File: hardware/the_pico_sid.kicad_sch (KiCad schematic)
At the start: 12 parts, among them J1 SWD, U1 SID_6581, U2 Pico, U3 4050, U4 4050

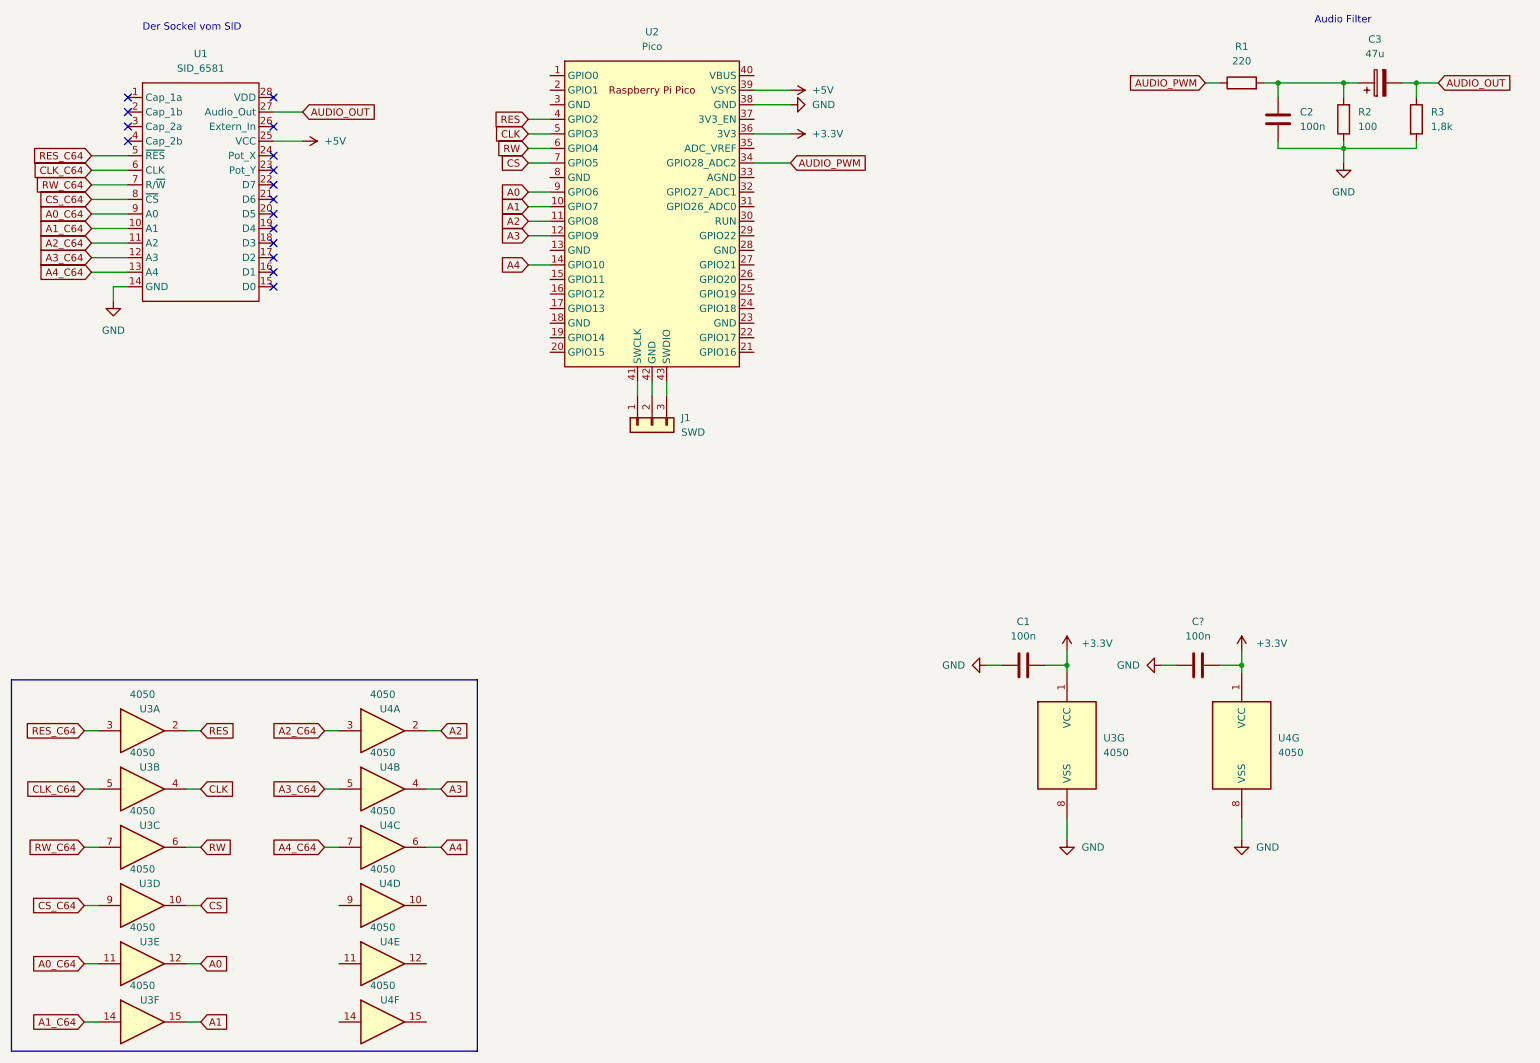
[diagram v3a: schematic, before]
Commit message: schematic: added data lines
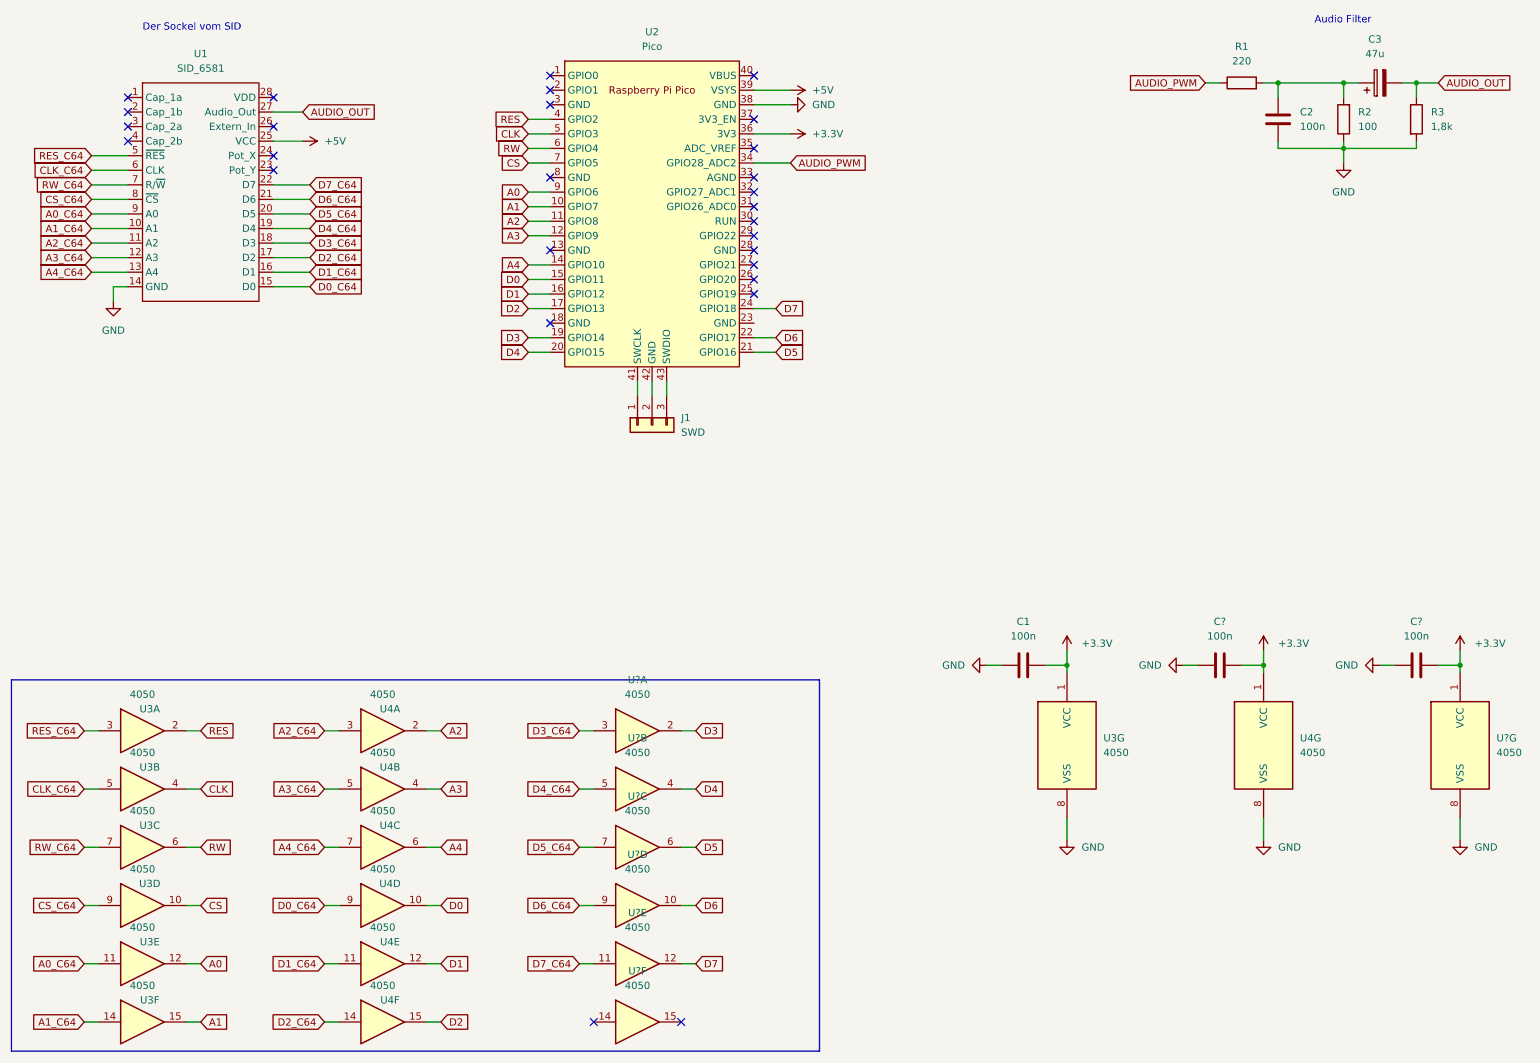
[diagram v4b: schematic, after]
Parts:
- added C?: 100n, symbol Device:C
- added U? (x7): 4050, symbol 4xxx:4050
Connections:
- net +3.3V: now also C?.2, U?.1 (VCC)
- net GND: now also C?.1, U?.8 (VSS)
- net D0: now reaches U4.10
- net D0: now also U2.15 (GPIO11)
- net D0_C64: now reaches U4.9
- net D0_C64: now also U1.15 (D0)
- net D2_C64: now reaches U4.14
- net D2_C64: now also U1.17 (D2)
- net D2: now reaches U4.15
- net D2: now also U2.17 (GPIO13)
- net D1_C64: now reaches U4.11
- net D1_C64: now also U1.16 (D1)
- net D1: now reaches U4.12
- net D1: now also U2.16 (GPIO12)
- net D3: now reaches U2.19 (GPIO14)
- net D3: now also U?.2
- net D4: now reaches U2.20 (GPIO15)
- net D4: now also U?.4
- net D5: now reaches U2.21 (GPIO16)
- net D5: now also U?.6
- net D6: now reaches U2.22 (GPIO17)
- net D6: now also U?.10
- net D7: now reaches U2.24 (GPIO18)
- net D7: now also U?.12
- net D3_C64: now reaches U1.18 (D3)
- net D3_C64: now also U?.3
- net D4_C64: now reaches U1.19 (D4)
- net D4_C64: now also U?.5
- net D5_C64: now reaches U1.20 (D5)
- net D5_C64: now also U?.7
- net D6_C64: now reaches U1.21 (D6)
- net D6_C64: now also U?.9
- net D7_C64: now reaches U1.22 (D7)
- net D7_C64: now also U?.11
- no-connect marks 16 -> 28
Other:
- moved on the sheet: C?, U4G

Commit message: Update the_pico_sid.kicad_sch
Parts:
- gave numbers to parts that had none: 3
- renumbered C2 to C3, C3 to C4, U3 to U1, U1 to U2, U4 to U3, U2 to U5

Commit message: Update the_pico_sid.kicad_sch
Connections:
- net CLK: now also U5.6 (GPIO4); no longer U5.5 (GPIO3)
- net CS: now also U5.5 (GPIO3); no longer U5.7 (GPIO5)
- net RW: now also U5.7 (GPIO5); no longer U5.6 (GPIO4)
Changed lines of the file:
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@@
     )
   )
-  (global_label "CS" (shape input) (at 104.14 40.64 180) (fields_autoplaced)
-    (effects (font (size 1.27 1.27)) (justify right))
-    (property "Referenzen zwischen Schaltplänen" "${INTERSHEET_REFS}" (id 0) (at 99.2474 40.7194 0)
+  (global_label "CS" (shape input) (at 104.14 35.56 180) (fields_autoplaced)
+    (effects (font (size 1.27 1.27)) (justify right))
+    (property "Referenzen zwischen Schaltplänen" "${INTERSHEET_REFS}" (id 0) (at 99.2474 35.6394 0)
       (effects (font (size 1.27 1.27)) (justify right) hide)
     )
@@
     )
   )
-  (global_label "RW" (shape input) (at 104.14 38.1 180) (fields_autoplaced)
-    (effects (font (size 1.27 1.27)) (justify right))
-    (property "Referenzen zwischen Schaltplänen" "${INTERSHEET_REFS}" (id 0) (at 99.0055 38.1794 0)
+  (global_label "RW" (shape input) (at 104.14 40.64 180) (fields_autoplaced)
+    (effects (font (size 1.27 1.27)) (justify right))
+    (property "Referenzen zwischen Schaltplänen" "${INTERSHEET_REFS}" (id 0) (at 99.0055 40.7194 0)
       (effects (font (size 1.27 1.27)) (justify right) hide)
     )
@@
     )
   )
-  (global_label "CLK" (shape input) (at 104.14 35.56 180) (fields_autoplaced)
-    (effects (font (size 1.27 1.27)) (justify right))
-    (property "Referenzen zwischen Schaltplänen" "${INTERSHEET_REFS}" (id 0) (at 98.1588 35.6394 0)
-      (effects (font (size 1.27 1.27)) (justify right) hide)
-    )
+  (global_label "CLK" (shape input) (at 104.14 38.1 180) (fields_autoplaced)
+    (effects (font (size 1.27 1.27)) (justify right))
+    (property "Referenzen zwischen Schaltplänen" "${INTERSHEET_REFS}" (id 0) (at 98.1588 38.1794 0)
+      (effects (font (size 1.27 1.27)) (justify right) hide)
+    )

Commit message: Update the_pico_sid.kicad_sch
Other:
- note added: "Funktioniert so leider nicht in meinem C64. AUDIO_PWM direkt am AUDIO_OUT der SID Sockels geht erstmal."
- moved on the sheet: C3, C4, R1, R2, R3

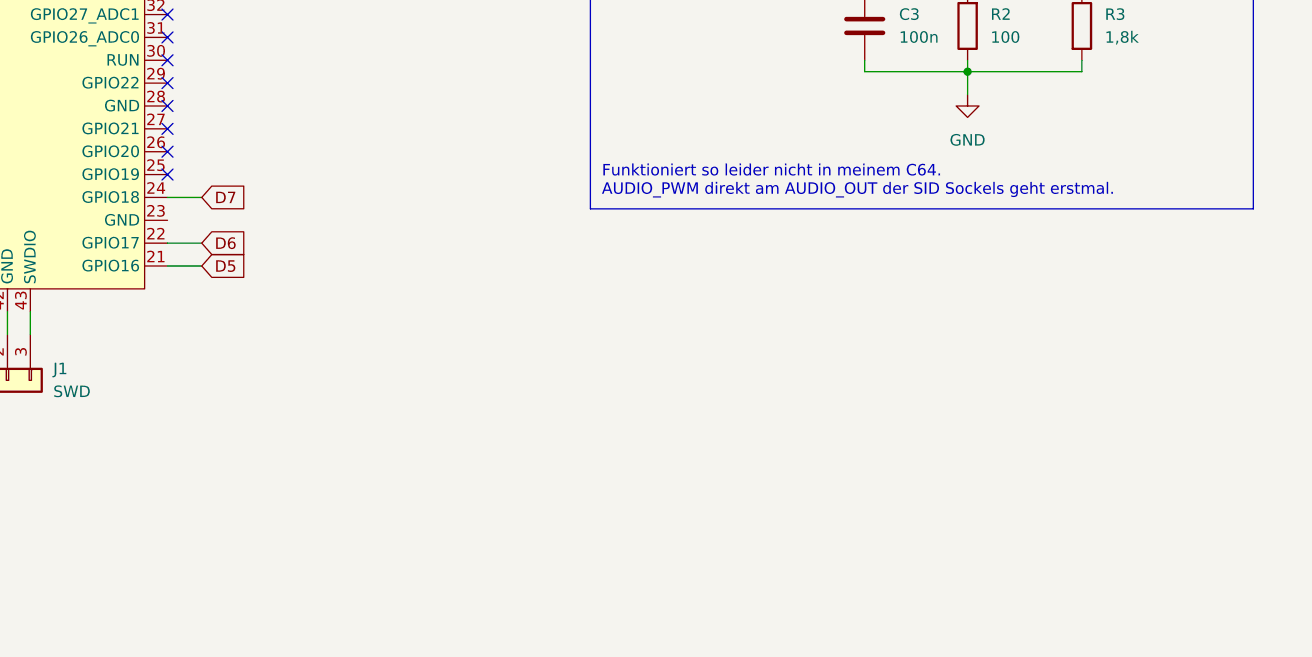
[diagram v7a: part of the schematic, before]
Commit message: schematic: add debug_led green or red status
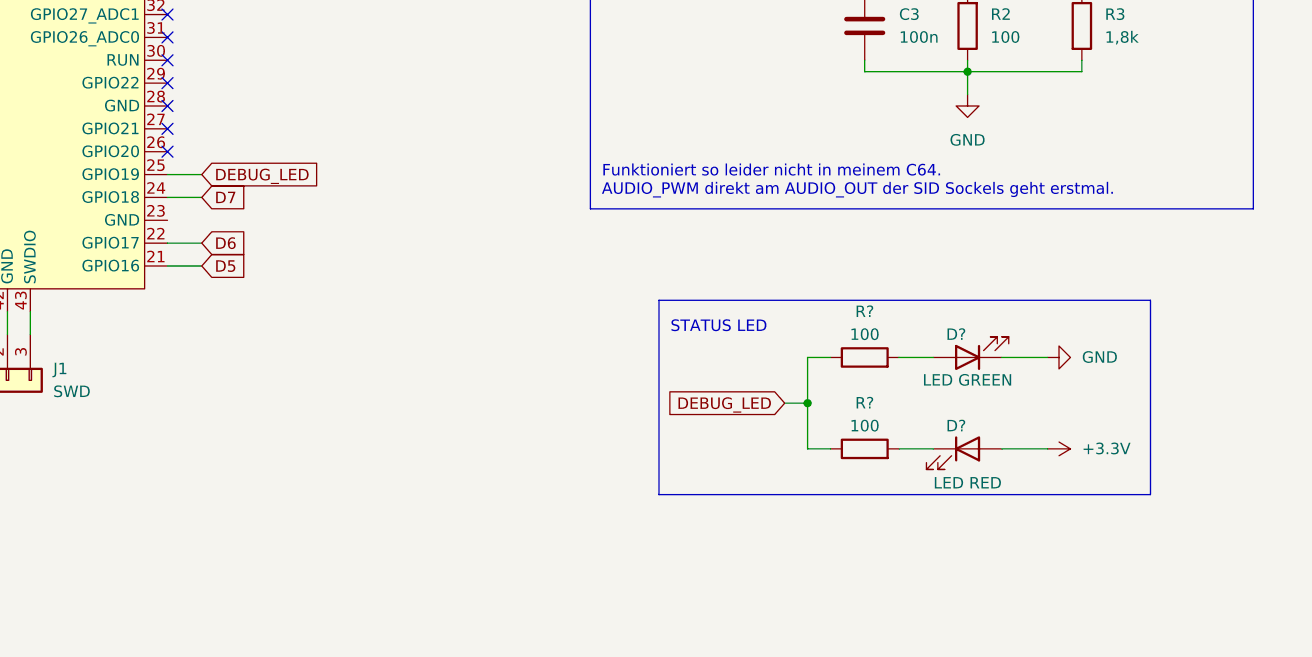
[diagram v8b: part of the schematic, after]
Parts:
- added D?: LED RED, symbol Device:LED
- added D?: LED GREEN, symbol Device:LED
- added R? (x2): 100, symbol Device:R
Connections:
- net +3.3V: now also D?.2 (A)
- net GND: now also D?.1 (K)
- net DEBUG_LED: now reaches U5.25 (GPIO19)
- net DEBUG_LED: now also R?.1, R?.1
- new net: D?.2 (A), R?.2
- new net: D?.1 (K), R?.2
- no-connect marks 28 -> 27
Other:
- note added: "STATUS LED"
